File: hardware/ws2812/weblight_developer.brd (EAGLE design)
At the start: 43.2 x 12 mm, 14 parts, among them U1 ATTiny85-20SU

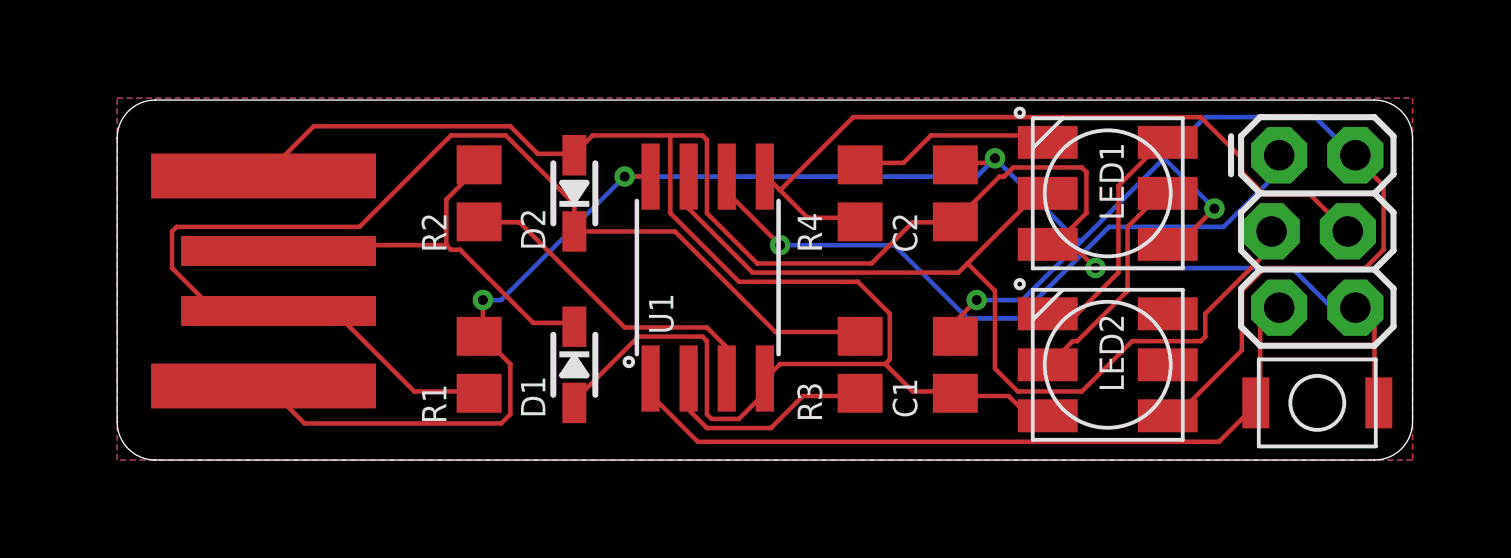
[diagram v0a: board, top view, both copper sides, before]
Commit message: Separate LED type and adopt new board versioning scheme
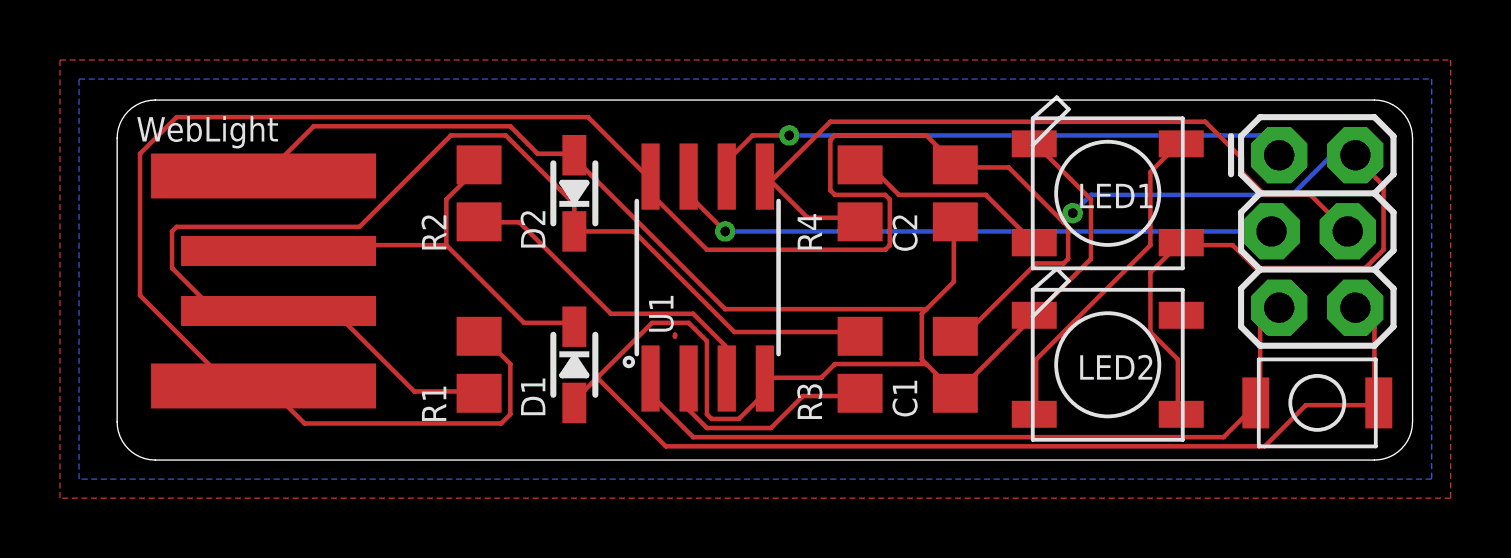
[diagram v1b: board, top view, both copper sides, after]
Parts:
- LED1, LED2: value APA102 -> WS2812B; device weblight:APA102 -> weblight:WS2812B
- turned LED1 to 0 degrees
- turned LED2 to 0 degrees
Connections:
- removed net SCK_1: JP1.3, LED1.CI, U1.7
- removed net SCK_2: LED1.CO, LED2.CI
- new net N$4: JP1.3, U1.7
- net DIN_1: now also LED1.4-DIN; no longer LED1.DI
- net DIN_2: now also LED1.2-DOUT, LED2.4-DIN; no longer LED1.DO, LED2.DI
- net GND: now also LED1.3-GND, LED2.3-GND; no longer LED1.GND, LED2.GND
- net VCC: now also LED1.1-VDD, LED2.1-VDD; no longer LED1.VCC, LED2.VCC
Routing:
- net SCK_1: track 31.4 -> 0.00 mm
- net VCC: track 74.3 -> 98.4 mm, vias 5 -> 1
- net N$4: track 0.00 -> 20.5 mm, vias 0 -> 1
- net SCK_2: track 7.69 -> 0.00 mm
- net GND: track 85.5 -> 90.8 mm, vias 1 -> 0
- net MISO: track 23.3 -> 19.6 mm
- net DIN_2: track 8.12 -> 11.1 mm
- added copper zone on layer 1, net GND
- added copper zone on layer 16, net GND
- removed copper zone on layer 16, net N$1
- removed copper zone on layer 1, net N$2
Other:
- board text added: "WebLight"
- board text added: "w-osh1"
- board text removed: "Version osh4"
